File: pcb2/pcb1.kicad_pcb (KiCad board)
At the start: 2 copper layers, 80 x 125 mm, 20 parts, among them J1 Input, J2 Output, Q1 IRFZ44N, U1 LM358

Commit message: make a board of with ne555
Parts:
- removed D1: 3.3V 500mA, Diode_THT:D_DO-35_SOD27_P7.62mm_Horizontal
- removed R1: 1k, Resistor_THT:R_Axial_DIN0207_L6.3mm_D2.5mm_P10.16mm_Horizontal
- removed Ra1: 2k, Resistor_THT:R_Axial_DIN0207_L6.3mm_D2.5mm_P10.16mm_Horizontal
- removed Rb1: 56R, Resistor_THT:R_Axial_DIN0207_L6.3mm_D2.5mm_P10.16mm_Horizontal
- added C4: 10nf, Capacitor_THT:C_Rect_L7.2mm_W6.0mm_P5.00mm, F.Cu at (96.3, 151.1)
- added C5: 10nf, Capacitor_THT:C_Rect_L7.2mm_W6.0mm_P5.00mm, F.Cu at (109.5, 136.8)
- added C6: 100nf, Capacitor_THT:C_Rect_L7.2mm_W6.0mm_P5.00mm, F.Cu at (99.5, 114.1)
- added R3: 10k, Resistor_THT:R_Axial_DIN0207_L6.3mm_D2.5mm_P10.16mm_Horizontal, F.Cu at (102.7, 160.3)
- added R5: 10k, Resistor_THT:R_Axial_DIN0207_L6.3mm_D2.5mm_P10.16mm_Horizontal, F.Cu at (102.7, 147.6)
- added R6: 100R, Resistor_THT:R_Axial_DIN0207_L6.3mm_D2.5mm_P10.16mm_Horizontal, F.Cu at (112.1, 130.6)
- added R7: 1k, Resistor_THT:R_Axial_DIN0207_L6.3mm_D2.5mm_P10.16mm_Horizontal, F.Cu at (98.4, 130.6)
- added R8: 10R, Resistor_THT:R_Axial_DIN0207_L6.3mm_D2.5mm_P10.16mm_Horizontal, F.Cu at (83.1, 101.4)
- added U2: NE555P, Package_DIP:DIP-8_W7.62mm, F.Cu at (90.2, 141.8)
- moved U1 15.8 mm to (99.4, 127.3)
- moved C1 6.31 mm to (56.4, 66.5)
- moved X1 6.31 mm to (107.8, 57.2)
- moved REF** 6.31 mm to (45.5, 45.5)
- moved C2 6.31 mm to (56.4, 103.1)
- moved C3 6.31 mm to (56.4, 139.6)
- moved D2 6.31 mm to (88.5, 104.0)
- moved Q1 6.31 mm to (94.7, 82.1)
- moved R2 6.31 mm to (105.0, 104.0)
- moved R4 6.31 mm to (110.3, 97.6)
- moved REF** 6.31 mm to (114.4, 159.3)
- moved REF** 6.31 mm to (45.4, 158.9)
- moved REF** 6.31 mm to (90.5, 79.6)
- moved REF** 6.31 mm to (114.4, 45.5)
- moved RSense1 6.31 mm to (85.4, 57.3)
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- renumbered J1 to X1, J2 to X2
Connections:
- U1 pad 1: Net-(Q1-G) -> Net-(U1B--)
- U1 pad 2: Net-(Q1-S) -> Net-(U1A--)
- U1 pad 3: Net-(U1A-+) -> Net-(Q1-S)
- U1 pad 5: GND -> Net-(U1B-+)
- U1 pad 6: GND -> Net-(U1B--)
- U1 pad 7: unconnected-(U1-Pad7) -> Net-(R8-Pad2)
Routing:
- net Net-(U1B-+): track 0.00 -> 83.9 mm, vias 0 -> 2
- net VCC: track 243.9 -> 308.7 mm
- net Net-(Q1-G): track 63.5 -> 35.5 mm
- net Net-(Q1-S): track 100.3 -> 126.9 mm
- net Net-(U1A-+): track 26.3 -> 0.00 mm
- net Net-(R8-Pad2): track 0.00 -> 24.1 mm
- net Net-(U1B--): track 0.00 -> 23.0 mm
- net Net-(U2-DISCH): track 0.00 -> 19.3 mm
- net Net-(U2-CONT): track 0.00 -> 16.6 mm
- net GND: track 161.5 -> 147.4 mm
- net Net-(D1-K): track 11.0 -> 0.00 mm
- net Net-(U1A--): track 0.00 -> 6.86 mm

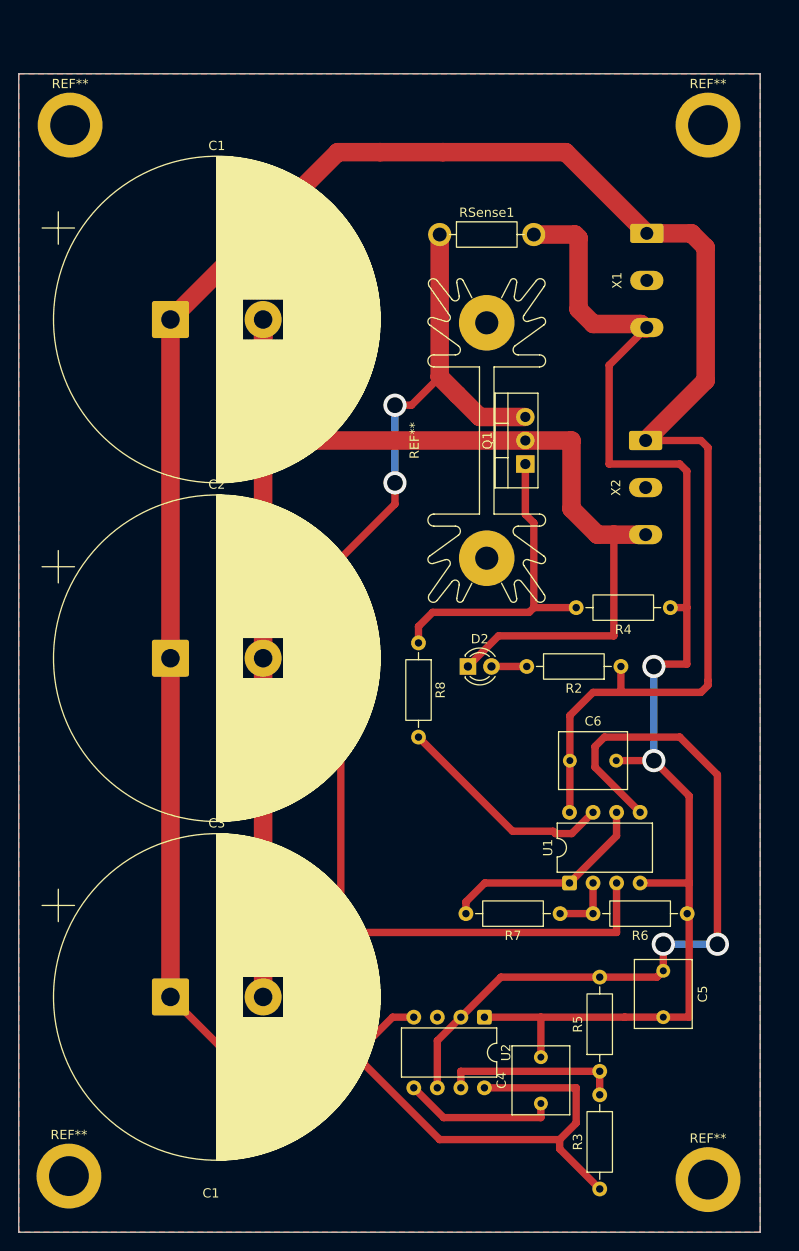
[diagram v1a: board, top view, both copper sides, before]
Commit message: add zener to stability
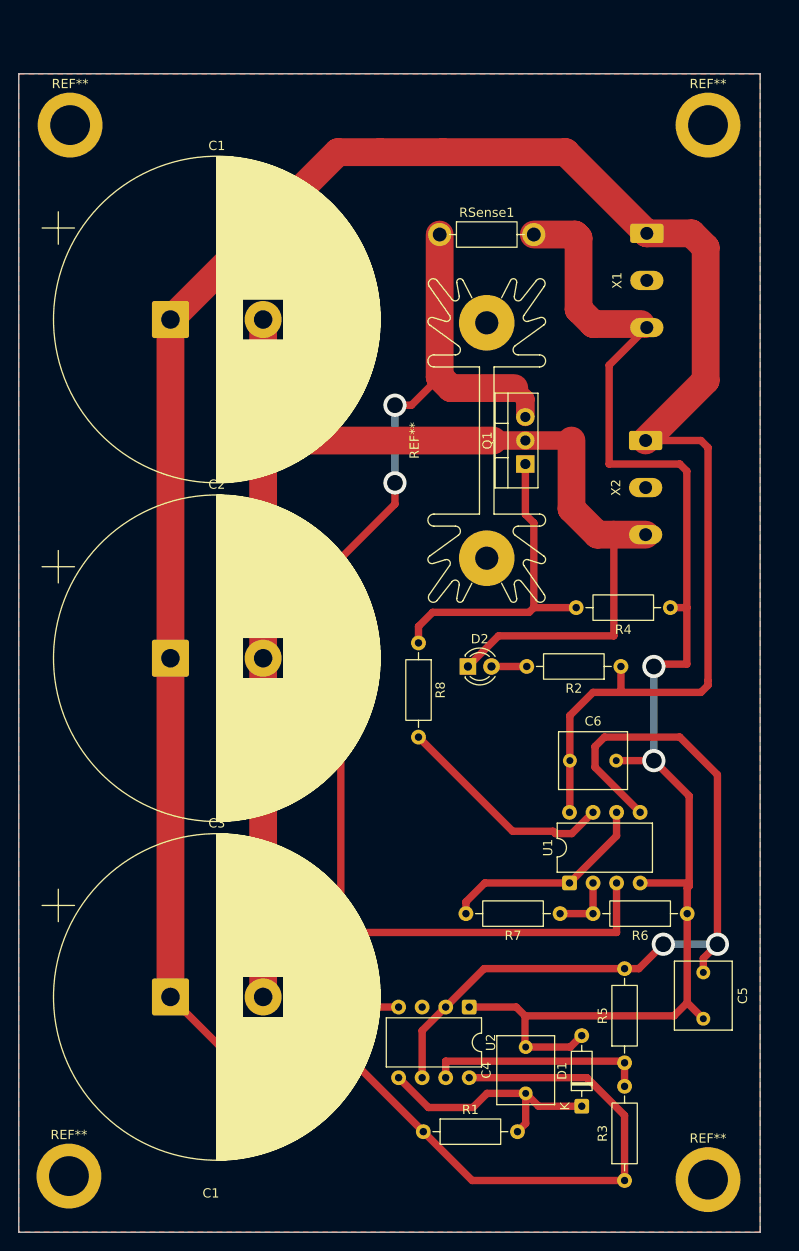
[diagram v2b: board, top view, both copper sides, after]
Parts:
- added D1: 8V2, Diode_THT:D_DO-35_SOD27_P7.62mm_Horizontal, F.Cu at (100.7, 151.4)
- added R1: 760R, Resistor_THT:R_Axial_DIN0207_L6.3mm_D2.5mm_P10.16mm_Horizontal, F.Cu at (83.7, 154.2)
- R6: value 100R -> 10R
- moved C5 4.32 mm to (113.9, 137.0)
- moved R3 2.83 mm to (105.4, 159.4)
- moved R5 2.83 mm to (105.4, 146.7)
- moved U2 1.97 mm to (88.6, 140.7)
- moved C4 1.97 mm to (94.7, 150.0)
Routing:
- net VCC: track 308.7 -> 320.3 mm
- net Net-(D1-K): track 16.6 -> 26.8 mm
- net GND: track 147.4 -> 156.4 mm
- net Net-(U2-DISCH): track 19.3 -> 23.7 mm
- net Net-(U1B-+): track 83.9 -> 87.0 mm
- net Net-(Q1-S): track 126.9 -> 128.0 mm

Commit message: ready to print
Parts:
- C4: footprint Capacitor_THT:C_Rect_L7.2mm_W6.0mm_P5.00mm -> Capacitor_THT:C_Rect_L7.2mm_W3.5mm_P5.00mm_FKS2_FKP2_MKS2_MKP2
- C5: footprint Capacitor_THT:C_Rect_L7.2mm_W6.0mm_P5.00mm -> Capacitor_THT:C_Rect_L7.0mm_W3.5mm_P5.00mm
- C6: footprint Capacitor_THT:C_Rect_L7.2mm_W6.0mm_P5.00mm -> Capacitor_THT:C_Rect_L9.0mm_W3.3mm_P7.50mm_MKT
- R1: value 760R -> 680R
- moved C3 2.06 mm to (55.6, 141.5)
- moved C1 1.95 mm to (55.6, 64.7)
- moved U2 1.74 mm to (90.3, 140.8)
- moved C2 0.77 mm to (55.6, 103.1)
- renumbered REF** to mount
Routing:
- net /load-: track 166.5 -> 202.3 mm
- net Net-(Q1-S): track 128.0 -> 119.1 mm
- net VCC: track 320.3 -> 326.5 mm
- net GND: track 156.4 -> 151.4 mm
- net Net-(U2-DISCH): track 23.7 -> 22.0 mm
- net Net-(D1-K): track 26.8 -> 26.0 mm
- net Net-(U1B-+): track 87.0 -> 86.4 mm
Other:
- board text removed: "C1"
